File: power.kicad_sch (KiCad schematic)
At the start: 16 parts, among them J3 Conn_01x02, Q1 SiS402DN, Q2 SiS402DN, U19 LM74502, U7 AMS1117-3.3, U8 AMS1117-5.0

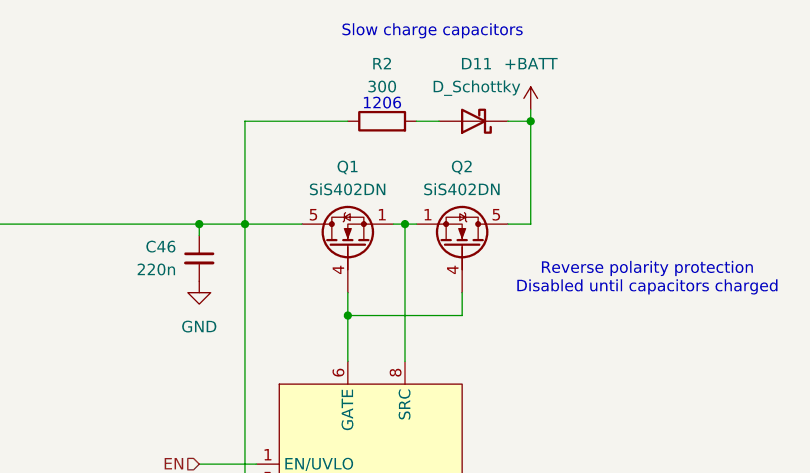
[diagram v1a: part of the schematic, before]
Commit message: switched around some footprints, added expansion header
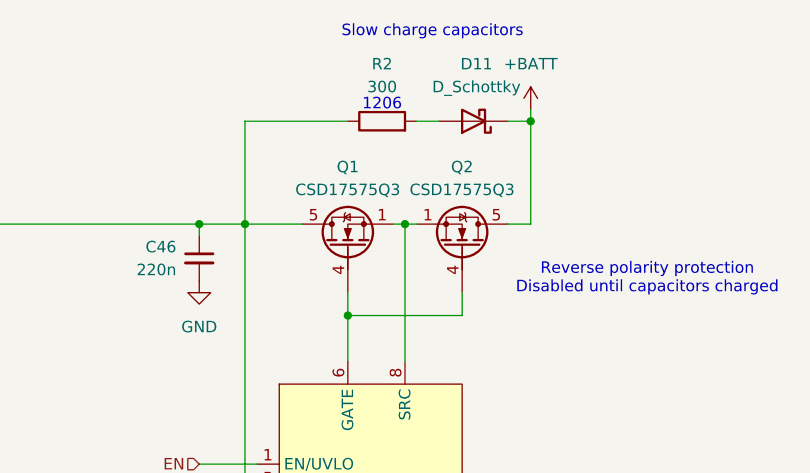
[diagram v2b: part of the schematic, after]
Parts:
- Q1, Q2: value SiS402DN -> CSD17575Q3; footprint Package_SO:Vishay_PowerPAK_1212-8_Single -> beavs-footprints:SON-8-1EP-3.3x3.3mm-nexfet; LCSC C15791 -> C529277
- U19: footprint Package_TO_SOT_SMD:SOT-23-8 -> beavs-footprints:SOT-23-8-THIN
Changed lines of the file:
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@@
 			)
 		)
-		(property "Value" "SiS402DN"
+		(property "Value" "CSD17575Q3"
 			(at 199.39 43.18 90)
 			(effects
@@
 			)
 		)
-		(property "Footprint" "Package_SO:Vishay_PowerPAK_1212-8_Single"
+		(property "Footprint" "beavs-footprints:SON-8-1EP-3.3x3.3mm-nexfet"
 			(at 196.85 44.45 0)
 			(effects
@@
 			)
 		)
-		(property "LCSC" "C15791"
+		(property "LCSC" "C529277"
 			(at 199.39 49.53 90)
 			(effects
@@
 			)
 		)
-		(property "Value" "SiS402DN"
+		(property "Value" "CSD17575Q3"
 			(at 212.09 43.18 90)
 			(effects
@@
 			)
 		)
-		(property "Footprint" "Package_SO:Vishay_PowerPAK_1212-8_Single"
+		(property "Footprint" "beavs-footprints:SON-8-1EP-3.3x3.3mm-nexfet"
 			(at 214.63 44.45 0)
 			(effects
@@
 			)
 		)
-		(property "LCSC" "C15791"
+		(property "LCSC" "C529277"
 			(at 212.09 49.53 90)
 			(effects
@@
 			)
 		)
-		(property "Footprint" "Package_TO_SOT_SMD:SOT-23-8"
+		(property "Footprint" "beavs-footprints:SOT-23-8-THIN"
 			(at 204.216 45.974 0)
 			(effects

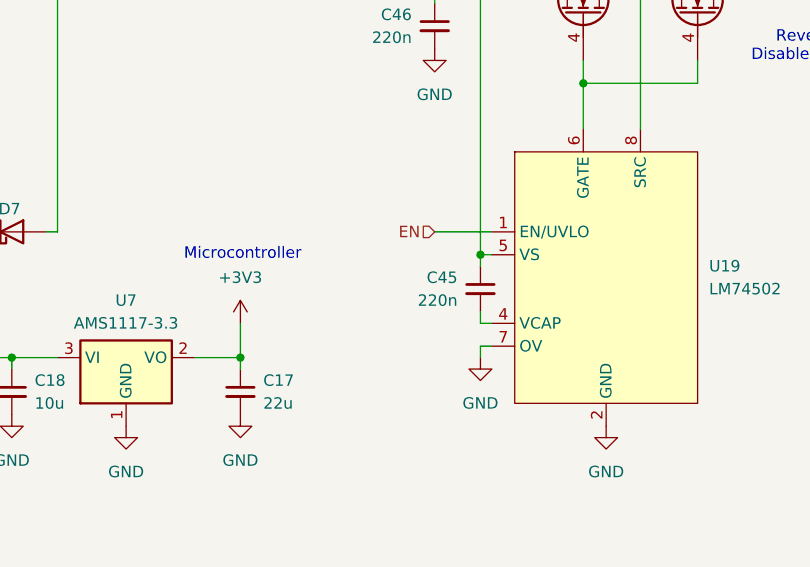
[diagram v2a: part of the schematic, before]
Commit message: fix pin order on FETs, cleanup
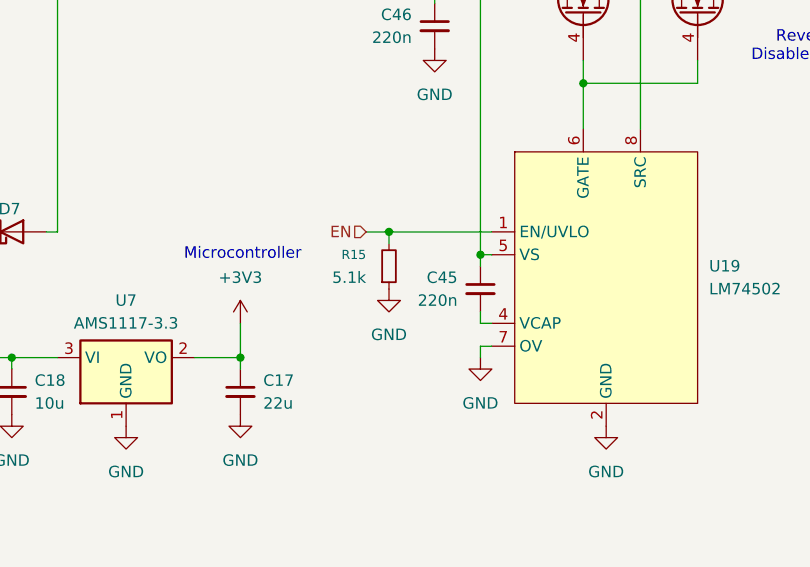
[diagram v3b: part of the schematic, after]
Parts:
- added R15: 5.1k, Resistor_SMD:R_0402_1005Metric, symbol Device:R_Small
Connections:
- net EN: now also R15.2
- net GND: now also R15.1
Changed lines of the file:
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@@
+	)
+	(junction
+		(at 177.8 73.66)
+		(diameter 0)
+		(color 0 0 0 0)
 	)
 	(junction
@@
 	(wire
 		(pts
-			(xy 182.88 73.66) (xy 189.23 73.66)
+			(xy 175.26 73.66) (xy 177.8 73.66)
 		)
 		(stroke
@@
 	(wire
 		(pts
+			(xy 177.8 73.66) (xy 189.23 73.66)
+		)
+		(stroke
+			(width 0)
+			(type default)
+		)
+	)
+	(wire
+		(pts
 			(xy 205.74 46.99) (xy 207.01 46.99)
 		)
@@
 		(pts
 			(xy 135.89 87.63) (xy 140.97 87.63)
+		)
+		(stroke
+			(width 0)
+			(type default)
+		)
+	)
+	(wire
+		(pts
+			(xy 177.8 73.66) (xy 177.8 74.93)
 		)
 		(stroke
@@
 	(hierarchical_label "EN"
 		(shape input)
-		(at 182.88 73.66 180)
+		(at 175.26 73.66 180)
 		(effects
 			(font
@@
 	)
 	(symbol
+		(lib_id "Device:R_Small")
+		(at 177.8 77.47 0)
+		(mirror x)
+		(unit 1)
+		(exclude_from_sim no)
+		(in_bom yes)
+		(on_board yes)
+		(dnp no)
+		(property "Reference" "R15"
+			(at 175.26 76.1999 0)
+			(effects
+				(font
+					(size 1.016 1.016)
+				)
+				(justify right)
+			)
+		)
+		(property "Value" "5.1k"
+			(at 175.26 78.7399 0)
+			(effects
+				(font
+					(size 1.27 1.27)
+				)
+				(justify right)
+			)
+		)
+		(property "Footprint" "Resistor_SMD:R_0402_1005Metric"
+			(at 177.8 77.47 0)
+			(effects
+				(font
+					(size 1.27 1.27)
+				)
+				(hide yes)
+			)
+		)
+		(property "Datasheet" "~"
+			(at 177.8 77.47 0)
+			(effects
+				(font
+					(size 1.27 1.27)
+				)
+				(hide yes)
+			)
+		)
+		(property "Description" "Resistor, small symbol"
+			(at 177.8 77.47 0)
+			(effects
+				(font
+					(size 1.27 1.27)
+				)
+				(hide yes)
+			)
+		)
+		(property "LCSC" "C25905"
+			(at 177.8 77.47 0)
+			(effects
+				(font
+					(size 1.27 1.27)
+				)
+				(hide yes)
+			)
+		)
+		(property "digikey" ""
+			(at 177.8 77.47 0)
+			(effects
+				(font
+					(size 1.27 1.27)
+				)
+				(hide yes)
+			)
+		)
+		(pin "2"
+		)
+		(pin "1"
+		)
+		(instances
+			(project "beavs-sketch-0"
+				(path "/49232f62-a438-4b3e-9be5-c2b3074d8de1/43b34b82-cf9c-4554-a5be-2b816c03d018"
+					(reference "R15")
+					(unit 1)
+				)
+			)
+		)
+	)
+	(symbol
 		(lib_id "Transistor_FET:Q_NMOS_SSSGD_AvalancheRated")
 		(at 212.09 49.53 270)
@@
 					(unit 1)
 				)
+			)
+		)
+	)
+	(symbol
+		(lib_id "power:GND")
+		(at 177.8 80.01 0)
+		(unit 1)
+		(exclude_from_sim no)
+		(in_bom yes)
+		(on_board yes)
+		(dnp no)
+		(fields_autoplaced yes)
+		(property "Reference" "#PWR0136"
+			(at 177.8 86.36 0)
+			(effects
+				(font
+					(size 1.27 1.27)
+				)
+				(hide yes)
+			)
+		)
+		(property "Value" "GND"
+			(at 177.8 85.09 0)
+			(effects
+				(font
+					(size 1.27 1.27)
+				)
+			)
+		)
+		(property "Footprint" ""
+			(at 177.8 80.01 0)
+			(effects
+				(font
+					(size 1.27 1.27)
+				)
+				(hide yes)
+			)
+		)
+		(property "Datasheet" ""
+			(at 177.8 80.01 0)
+			(effects
+				(font
+					(size 1.27 1.27)
+				)
+				(hide yes)
+			)
+		)
+		(property "Description" "Power symbol creates a global label with name \"GND\" , ground"
+			(at 177.8 80.01 0)
+			(effects
+				(font
+					(size 1.27 1.27)
+				)
+				(hide yes)
+			)
+		)
+		(pin "1"
+		)
+		(instances
+			(project ""
+				(path "/49232f62-a438-4b3e-9be5-c2b3074d8de1/43b34b82-cf9c-4554-a5be-2b816c03d018"
+					(reference "#PWR0136")
+					(unit 1)
+				)
